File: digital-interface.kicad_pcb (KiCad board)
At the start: 2 copper layers, 33 parts, among them U701 Si8641BD-B-IS2, U702 R05C05TE05S

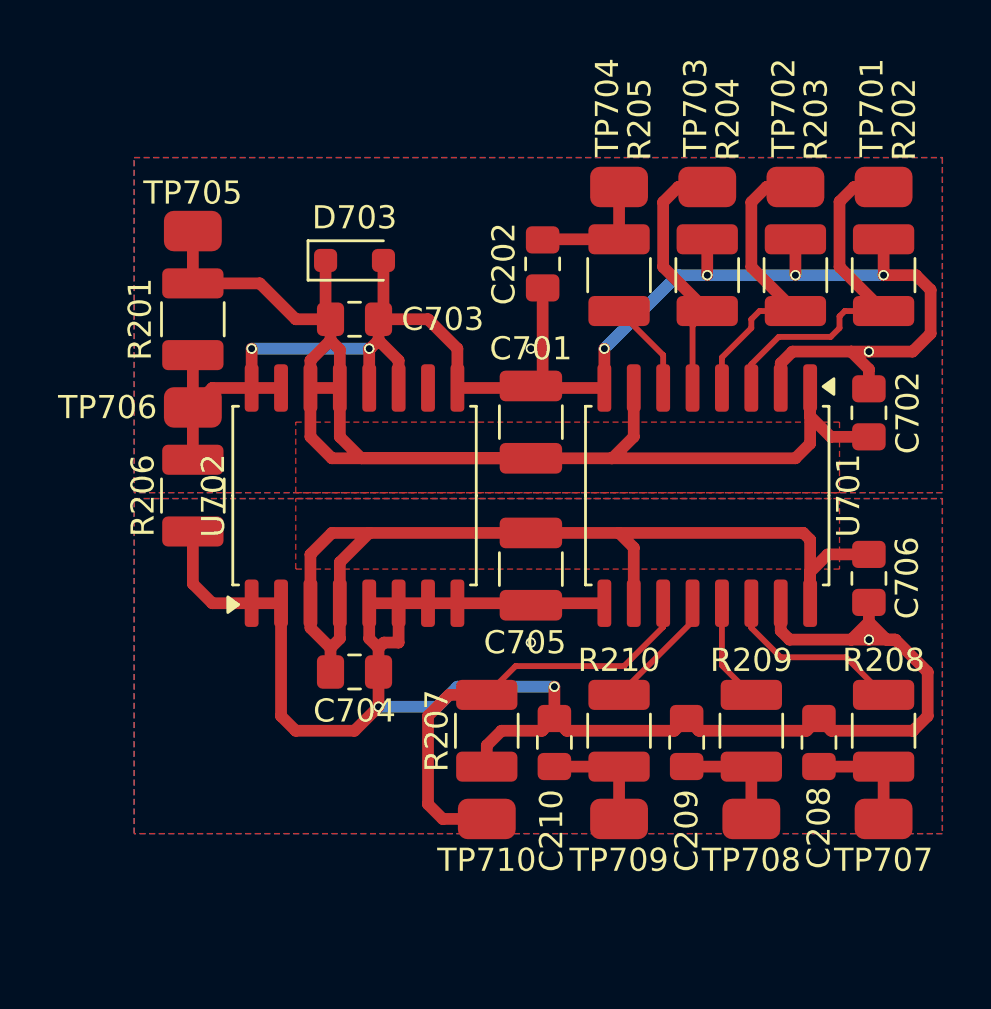
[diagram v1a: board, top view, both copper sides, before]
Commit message: enhance silk screen
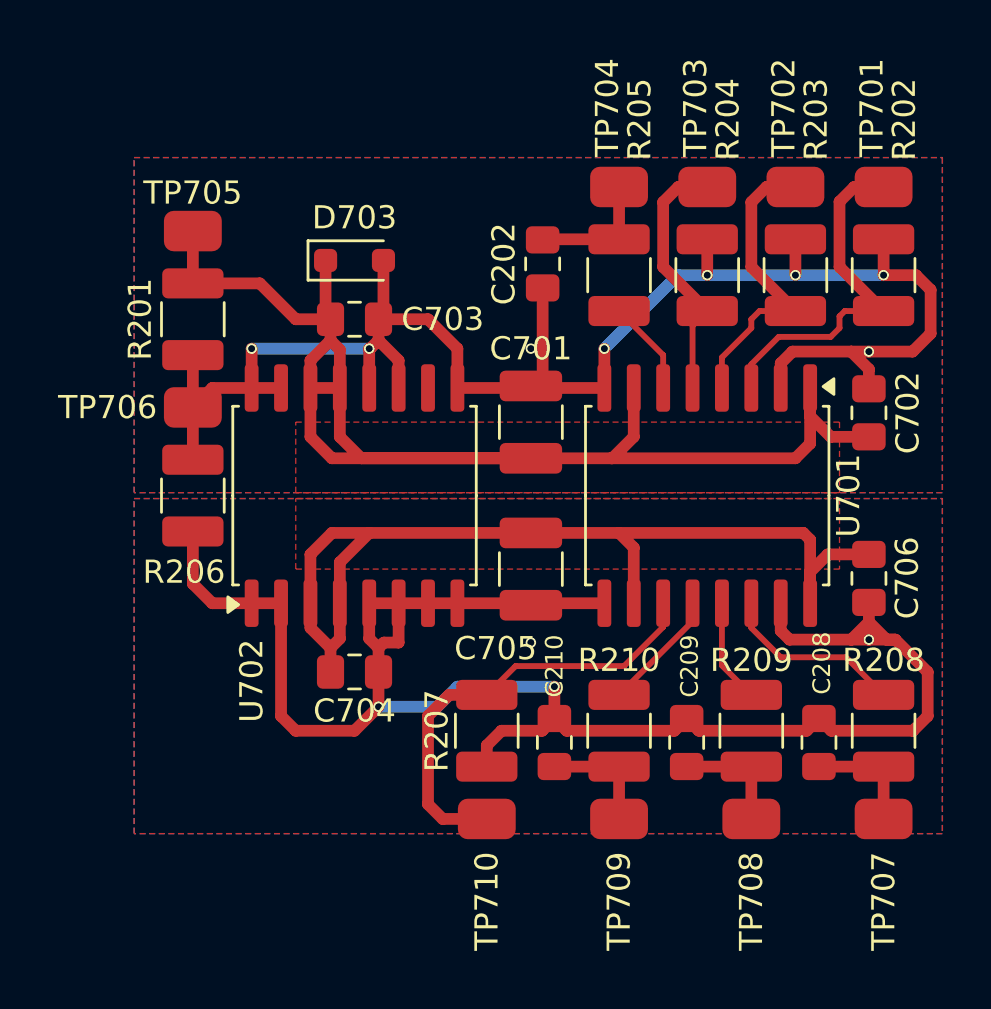
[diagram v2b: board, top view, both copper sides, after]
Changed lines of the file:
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@@
 		(tags "capacitor handsolder")
 		(property "Reference" "C209"
-			(at 3.81 0 90)
+			(at -3.302 -0.127 90)
 			(layer "F.SilkS")
 			(effects
 				(font
-					(size 1 1)
+					(size 0.762 0.762)
 					(thickness 0.15)
 				)
@@
 		(tags "resistor")
 		(property "Reference" "TP708"
-			(at 0 1.778 0)
+			(at 0 3.556 90)
 			(layer "F.SilkS")
 			(effects
@@
 		(tags "SOIC SO")
 		(property "Reference" "U702"
-			(at 0 -6.1 -90)
+			(at -8.001 -4.445 -90)
 			(layer "F.SilkS")
 			(effects
@@
 		(tags "resistor")
 		(property "Reference" "TP710"
-			(at 0 1.778 0)
+			(at 0 3.556 90)
 			(layer "F.SilkS")
 			(effects
@@
 		(tags "capacitor handsolder")
 		(property "Reference" "C705"
-			(at -3.175 -0.254 0)
+			(at -3.429 -1.524 0)
 			(layer "F.SilkS")
 			(effects
@@
 		(tags "resistor handsolder")
 		(property "Reference" "R206"
-			(at 0 2.159 90)
+			(at 3.302 0.381 180)
 			(layer "F.SilkS")
 			(effects
@@
 		(tags "resistor")
 		(property "Reference" "TP709"
-			(at 0 1.778 0)
+			(at 0 3.556 90)
 			(layer "F.SilkS")
 			(effects
@@
 		(tags "capacitor handsolder")
 		(property "Reference" "C208"
-			(at 3.683 0 90)
+			(at -3.429 -0.127 90)
 			(layer "F.SilkS")
 			(effects
 				(font
-					(size 1 1)
+					(size 0.762 0.762)
 					(thickness 0.15)
 				)
@@
 		(tags "capacitor handsolder")
 		(property "Reference" "C210"
-			(at 3.81 0.127 90)
+			(at -3.302 0 90)
 			(layer "F.SilkS")
 			(effects
 				(font
-					(size 1 1)
+					(size 0.762 0.762)
 					(thickness 0.15)
 				)
@@
 		(tags "resistor")
 		(property "Reference" "TP707"
-			(at 0 1.778 0)
+			(at 0 3.556 90)
 			(layer "F.SilkS")
 			(effects

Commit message: fix drc errors
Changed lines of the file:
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@@
 			(effects
 				(font
-					(size 0.762 0.762)
+					(size 0.8001 0.762)
 					(thickness 0.15)
 				)
@@
 			(effects
 				(font
-					(size 0.762 0.762)
+					(size 0.8001 0.762)
 					(thickness 0.15)
 				)
@@
 			(effects
 				(font
-					(size 0.762 0.762)
+					(size 0.8001 0.762)
 					(thickness 0.15)
 				)
